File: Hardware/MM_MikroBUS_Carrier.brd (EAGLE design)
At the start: 85.1 x 35.6 mm, 90 parts, among them J15 MICROMOD-2222-C, J2 QWIIC_RIGHT_ANGLE, J5 Vertical Qwiic Connector, J7 MIKROBUS_SMD_BLACK1, U1 MCP73831, U2 AP7361C-33FGEUDFN-8

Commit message: Add HW test sketch
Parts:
- moved U$17 2.54 mm to (33.0, 30.5)
- moved U$18 2.54 mm to (33.0, 30.5)
- moved U$20 2.54 mm to (30.5, 30.7)
- moved U$21 2.54 mm to (30.5, 30.7)
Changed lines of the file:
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@@
 <?xml version="1.0" encoding="utf-8"?>
 <!DOCTYPE eagle SYSTEM "eagle.dtd">
-<eagle version="9.4.2">
+<eagle version="9.5.2">
 <drawing>
 <settings>
-<setting alwaysvectorfont="yes"/>
+<setting alwaysvectorfont="no"/>
 <setting verticaltext="up"/>
 </settings>
@@
 <layer number="23" name="tOrigins" color="15" fill="1" visible="yes" active="yes"/>
 <layer number="24" name="bOrigins" color="15" fill="1" visible="yes" active="yes"/>
-<layer number="25" name="tNames" color="7" fill="1" visible="yes" active="yes"/>
+<layer number="25" name="tNames" color="7" fill="1" visible="no" active="yes"/>
 <layer number="26" name="bNames" color="7" fill="1" visible="no" active="yes"/>
-<layer number="27" name="tValues" color="7" fill="1" visible="yes" active="yes"/>
+<layer number="27" name="tValues" color="7" fill="1" visible="no" active="yes"/>
 <layer number="28" name="bValues" color="7" fill="1" visible="no" active="yes"/>
 <layer number="29" name="tStop" color="7" fill="3" visible="no" active="yes"/>
@@
 <element name="U$36" library="buzzard_labels (1)" package="#0" value="" x="1.143" y="17.399" smashed="yes"/>
 <element name="U$37" library="buzzard_labels (1)" package="#0" value="" x="7.366" y="23.495" smashed="yes"/>
-<element name="U$17" library="output" package="#D0#0" value="" x="30.48" y="30.48" smashed="yes" rot="R90"/>
-<element name="U$18" library="output" package="#D0#0" value="" x="30.48" y="30.48" smashed="yes" rot="MR90"/>
-<element name="U$20" library="output" package="#D1#0" value="" x="33.02" y="30.734" smashed="yes" rot="R90"/>
-<element name="U$21" library="output" package="#D1#0" value="" x="33.02" y="30.734" smashed="yes" rot="MR90"/>
+<element name="U$17" library="output" package="#D0#0" value="" x="33.02" y="30.48" smashed="yes" rot="R90"/>
+<element name="U$18" library="output" package="#D0#0" value="" x="33.02" y="30.48" smashed="yes" rot="MR90"/>
+<element name="U$20" library="output" package="#D1#0" value="" x="30.48" y="30.734" smashed="yes" rot="R90"/>
+<element name="U$21" library="output" package="#D1#0" value="" x="30.48" y="30.734" smashed="yes" rot="MR90"/>
 <element name="J6" library="SparkFun-Connectors" package="1X09_NO_SILK" value="" x="22.86" y="34.29" smashed="yes">
 <attribute name="NAME" x="21.59" y="35.687" size="0.6096" layer="25" font="vector" ratio="20"/>

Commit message: Updating with mikroE suggestions
* "mikroBUS" label, not "MikroBUS"
* Add pin names to socket
* Change button labeling to "Mikroe Reset"
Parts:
- added U$1: (no value), output:MIKROE0
- added U$40: (no value), output:RST0
- added U$41: (no value), output:CS0
- added U$42: (no value), output:SCK0
- added U$43: (no value), output:CIPO0
- added U$45: (no value), output:COPI0
- added U$46: (no value), output:3#3V0
- added U$47, U$48: (no value), output:GND0
- added U$49: (no value), output:PWM0
- added U$50: (no value), output:INT0
- added U$51: (no value), output:RX0
- added U$52: (no value), output:TX0
- added U$53: (no value), output:SCL0
- added U$54: (no value), output:SDA0
- added U$55: (no value), output:VIN0
- U$35: device output:MIKROBUS_CARRIER0 -> output:AN0
- U$5: device output:MIK0 -> output:MIKROBUS_CARRIER0
- moved U$5 29.8 mm to (57.5, 1.65), turned to 0 degrees
- moved U$38 23.7 mm to (76.8, 15.1), flipped to the bottom
- moved U$35 11.6 mm to (74.9, 26.7), flipped to the top, turned to 270 degrees
- moved LOGO2 0.25 mm to (55.3, 1.65)
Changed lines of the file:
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@@
 <?xml version="1.0" encoding="utf-8"?>
 <!DOCTYPE eagle SYSTEM "eagle.dtd">
-<eagle version="9.5.2">
+<eagle version="9.4.2">
 <drawing>
 <settings>
-<setting alwaysvectorfont="no"/>
+<setting alwaysvectorfont="yes"/>
 <setting verticaltext="up"/>
 </settings>
@@
 <attribute name="VALUE" x="23.495" y="5.969" size="0.6096" layer="27" font="vector" ratio="20" rot="R180" align="top-center"/>
 </element>
-<element name="LOGO2" library="SparkFun-Aesthetics" package="QWIIC_5.5MM" value="QWIIC_LOGO_CONNECTOR" x="55.3085" y="1.397" smashed="yes"/>
+<element name="LOGO2" library="SparkFun-Aesthetics" package="QWIIC_5.5MM" value="QWIIC_LOGO_CONNECTOR" x="55.3085" y="1.651" smashed="yes"/>
 <element name="LOGO3" library="SparkFun-Aesthetics" package="OSHW-LOGO-M" value="OSHW-LOGOM" x="62.23" y="9.906" smashed="yes" rot="MR0"/>
 <element name="H5" library="SparkFun-Hardware" package="STAND-OFF-REFLOW-M2.5" value="STAND-OFF-REFLOW-M2.5_2.5MM_TALL" x="44.327" y="13.76" smashed="yes">
@@
 <element name="U$19" library="output" package="#3V3_#0" value="" x="20.828" y="33.655" smashed="yes" rot="MR0"/>
 <element name="U$6" library="output" package="#3V3_EN#0" value="" x="15.748" y="16.51" smashed="yes" rot="MR0"/>
-<element name="U$35" library="output" package="MIKROBUS_CARRIER0" value="" x="74.422" y="15.113" smashed="yes" rot="MR0"/>
-<element name="U$38" library="output" package="_MIKROBUS_CARRIER0" value="" x="57.277" y="1.651" smashed="yes"/>
-<element name="U$5" library="output" package="MIK0" value="" x="27.686" y="1.397" smashed="yes" rot="R90"/>
 <element name="U$39" library="output" package="RESET0" value="" x="28.829" y="0.508" smashed="yes" rot="R90"/>
+<element name="U$1" library="output" package="MIKROE0" value="" x="27.686" y="0.127" smashed="yes" rot="R90"/>
+<element name="U$5" library="output" package="MIKROBUS_CARRIER0" value="" x="57.531" y="1.651" smashed="yes"/>
+<element name="U$38" library="output" package="_MIKROBUS_CARRIER0" value="" x="76.835" y="15.113" smashed="yes" rot="MR0"/>
+<element name="U$35" library="output" package="AN0" value="" x="74.93" y="26.67" smashed="yes" rot="R270"/>
+<element name="U$40" library="output" package="RST0" value="" x="72.39" y="26.67" smashed="yes" rot="R270"/>
+<element name="U$41" library="output" package="CS0" value="" x="69.85" y="26.67" smashed="yes" rot="R270"/>
+<element name="U$42" library="output" package="SCK0" value="" x="67.31" y="26.67" smashed="yes" rot="R270"/>
+<element name="U$43" library="output" package="CIPO0" value="" x="64.77" y="26.67" smashed="yes" rot="R270"/>
+<element name="U$45" library="output" package="COPI0" value="" x="62.23" y="26.67" smashed="yes" rot="R270"/>
+<element name="U$46" library="output" package="3#3V0" value="" x="59.69" y="26.67" smashed="yes" rot="R270"/>
+<element name="U$47" library="output" package="GND0" value="" x="57.15" y="26.67" smashed="yes" rot="R270"/>
+<element name="U$48" library="output" package="GND0" value="" x="57.15" y="12.954" smashed="yes" rot="R270"/>
+<element name="U$49" library="output" package="PWM0" value="" x="74.93" y="13.589" smashed="yes" rot="R270"/>
+<element name="U$50" library="output" package="INT0" value="" x="72.39" y="12.446" smashed="yes" rot="R270"/>
+<element name="U$51" library="output" package="RX0" value="" x="69.85" y="11.938" smashed="yes" rot="R270"/>
+<element name="U$52" library="output" package="TX0" value="" x="67.31" y="12.192" smashed="yes" rot="R270"/>
+<element name="U$53" library="output" package="SCL0" value="" x="64.77" y="12.7" smashed="yes" rot="R270"/>
+<element name="U$54" library="output" package="SDA0" value="" x="62.23" y="12.954" smashed="yes" rot="R270"/>
+<element name="U$55" library="output" package="VIN0" value="" x="59.69" y="12.573" smashed="yes" rot="R270"/>
 </elements>
 <signals>
@@
 <contactref element="S3" pad="2"/>
 <via x="57.15" y="28.321" extent="1-16" drill="0.3048"/>
-<via x="57.15" y="6.858" extent="1-16" drill="0.3048"/>
+<via x="58.039" y="2.921" extent="1-16" drill="0.3048"/>
 <via x="33.02" y="1.27" extent="1-16" drill="0.3048"/>
 <via x="50.292" y="2.286" extent="1-16" drill="0.3048"/>

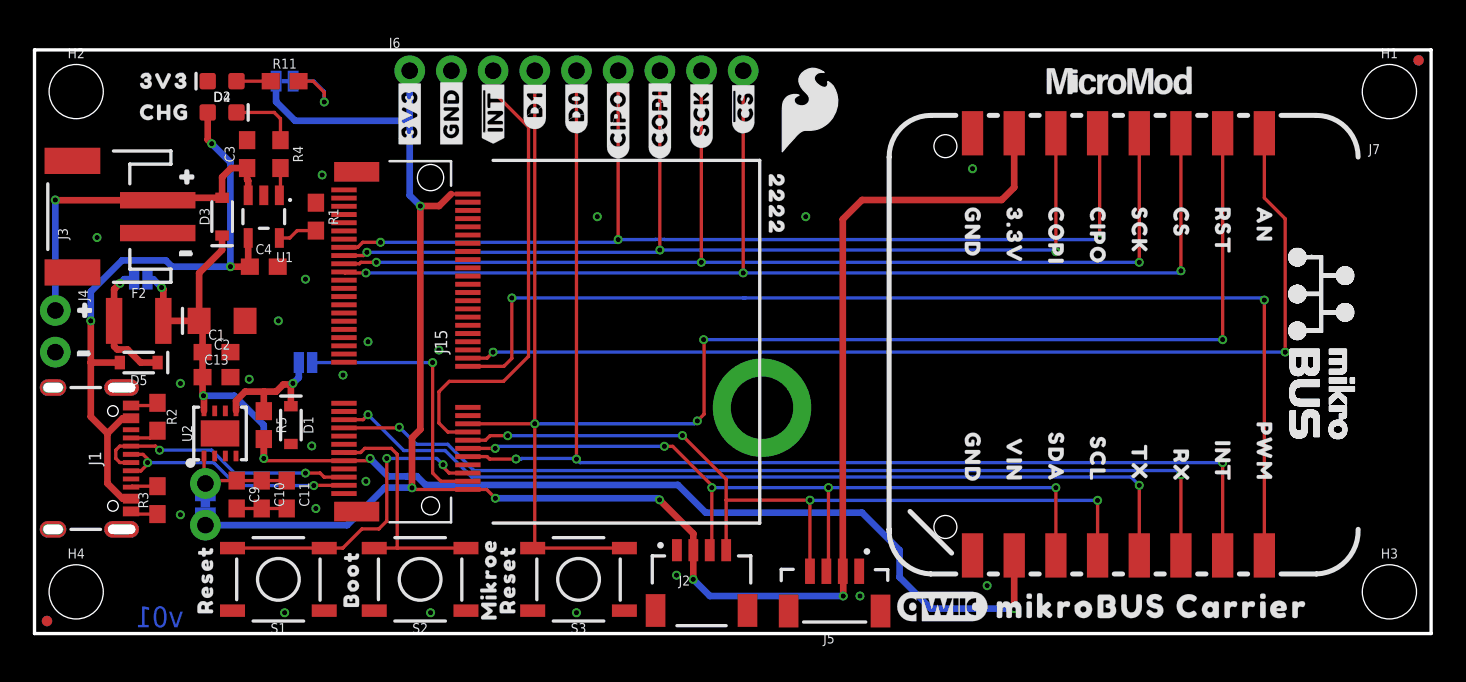
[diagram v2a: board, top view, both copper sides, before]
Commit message: MikroE updates
* Add JTAG connector
* Remove mikroE reset button
* Moved mikroBUS labels so that they can all be seen when socket is populated
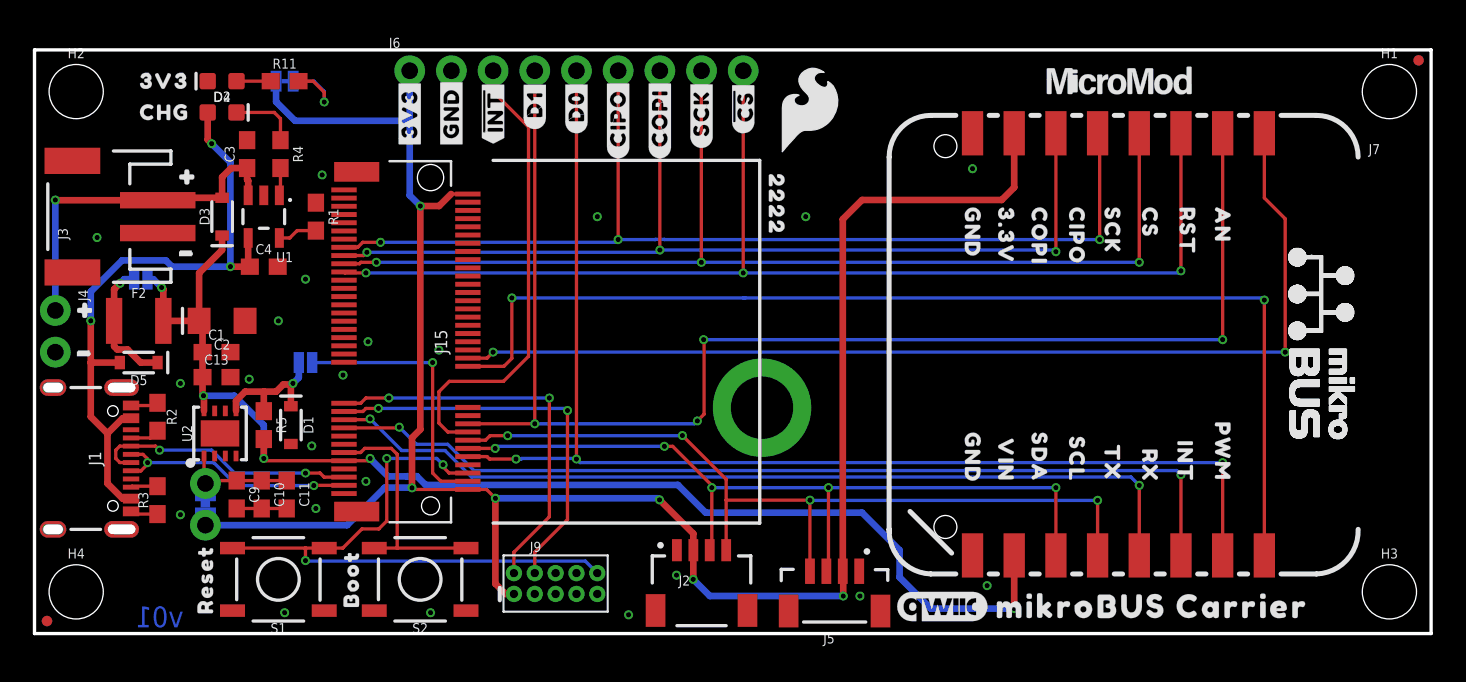
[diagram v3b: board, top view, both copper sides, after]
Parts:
- removed S3: MIK_RESET, SparkFun-Switches:TACTILE_SWITCH_SMD_5.2MM
- removed U$1: (no value), output:MIKROE0
- removed U$39: (no value), output:RESET0
- added J9: CORTEX_JTAG_DEBUG_MINIMUM_PTH, SparkFun-Connectors:2X5-PTH-1.27MM
- moved U$35 2.54 mm to (72.4, 26.7)
- moved U$49 2.54 mm to (72.4, 13.6)
- moved U$50 2.29 mm to (70.1, 12.4)
- moved U$40 2.16 mm to (70.2, 26.7)
- moved U$41 1.91 mm to (67.9, 26.7)
- moved U$51 1.91 mm to (67.9, 11.9)
- moved U$42 1.65 mm to (65.7, 26.7)
- moved U$52 1.65 mm to (65.7, 12.2)
- moved U$43 1.27 mm to (63.5, 26.7)
- moved U$53 1.27 mm to (63.5, 12.7)
- moved U$45 1.02 mm to (61.2, 26.7)
- moved U$54 1.02 mm to (61.2, 13.0)
- moved U$46 0.51 mm to (59.2, 26.7)
- moved U$55 0.51 mm to (59.2, 12.6)
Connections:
- new net SWDCK: J15.21, J9.4
- new net SWDIO: J15.23, J9.2
- net !RESET!: now also J9.10
- net 3.3V: now also J9.1
- net GND: now also J9.3, J9.5, J9.9; no longer S3.1, S3.2
- net MIK_RST: no longer S3.3, S3.4
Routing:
- net SWDCK: track 0.00 -> 24.5 mm, vias 0 -> 2
- net SWDIO: track 0.00 -> 24.2 mm, vias 0 -> 2
- net !RESET!: track 19.3 -> 38.1 mm, vias 2 -> 3
- net MIK_RST: track 98.1 -> 84.9 mm
- net 3.3V: track 121.4 -> 128.0 mm

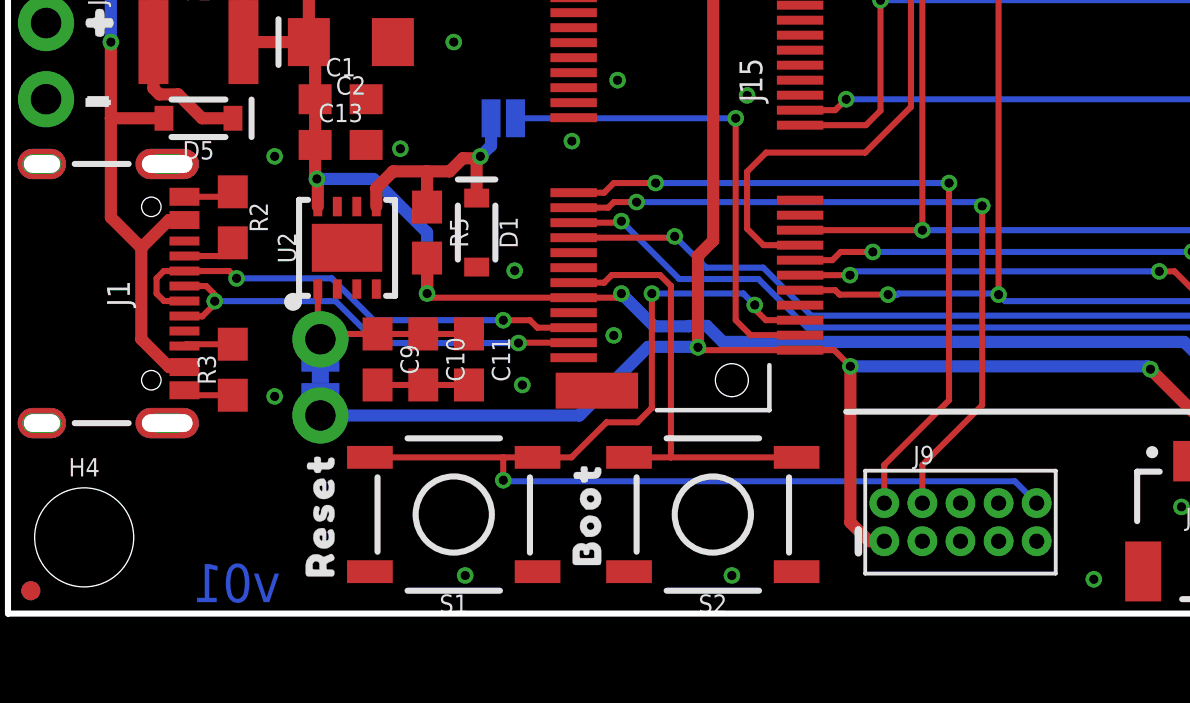
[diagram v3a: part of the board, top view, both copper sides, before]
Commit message: Pete's updates
* Bump version number on schematic and board
* Add measures for header
* Add test points for SWDIO and SWDCK
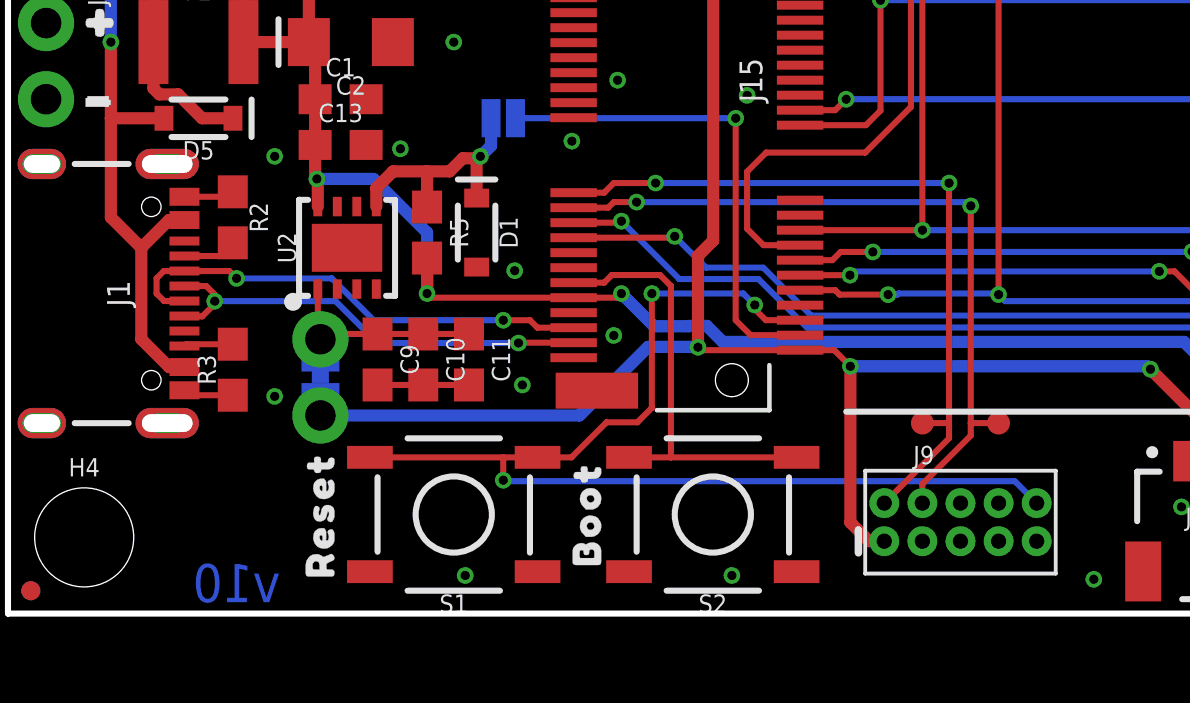
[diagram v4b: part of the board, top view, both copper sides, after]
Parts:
- added SWDCK, SWDIO: TEST-POINT3, SparkFun-Connectors:PAD.03X.03
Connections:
- net SWDCK: now also SWDCK.1
- net SWDIO: now also SWDIO.1
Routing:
- net SWDIO: track 24.2 -> 25.1 mm
- net SWDCK: track 24.5 -> 25.1 mm
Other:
- board text added: "v10"
- board text removed: "v01"
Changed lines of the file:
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@@
 <layer number="45" name="Holes" color="7" fill="1" visible="yes" active="yes"/>
 <layer number="46" name="Milling" color="3" fill="1" visible="no" active="yes"/>
-<layer number="47" name="Measures" color="7" fill="1" visible="no" active="yes"/>
+<layer number="47" name="Measures" color="7" fill="1" visible="yes" active="yes"/>
 <layer number="48" name="Document" color="7" fill="1" visible="no" active="yes"/>
 <layer number="49" name="Reference" color="7" fill="1" visible="no" active="yes"/>
@@
 <wire x1="85.09" y1="35.56" x2="85.09" y2="0" width="0.2032" layer="20"/>
 <wire x1="85.09" y1="0" x2="0" y2="0" width="0.2032" layer="20"/>
-<text x="7.62" y="1.016" size="1.27" layer="16" font="vector" ratio="20" rot="MR180" align="center">v01</text>
+<text x="7.62" y="1.016" size="1.27" layer="16" font="vector" ratio="20" rot="MR180" align="center">v10</text>
 <wire x1="27.94" y1="28.829" x2="44.185" y2="28.829" width="0.2032" layer="21"/>
 <wire x1="44.185" y1="28.829" x2="44.185" y2="6.731" width="0.2032" layer="21"/>
@@
 <text x="93.091" y="22.86" size="1.778" layer="47" font="vector" ratio="15" rot="R270">in</text>
 <text x="85.344" y="16.637" size="1.778" layer="47" font="vector" ratio="15" rot="R270">in</text>
-<text x="45.974" y="38.735" size="1.778" layer="47" font="vector" ratio="15">in</text>
-<text x="45.974" y="43.688" size="1.778" layer="47" font="vector" ratio="15">in</text>
+<text x="45.974" y="45.085" size="1.778" layer="47" font="vector" ratio="15">in</text>
+<text x="45.974" y="41.148" size="1.778" layer="47" font="vector" ratio="15">in</text>
 <dimension x1="0" y1="0" x2="6.223" y2="10.668" x3="-2.54" y3="5.334" textsize="1.778" textratio="15" layer="47" dtype="vertical" unit="inch"/>
 <dimension x1="0" y1="0" x2="3.81" y2="25.4" x3="-6.35" y3="12.7" textsize="1.778" textratio="15" layer="47" dtype="vertical" unit="inch"/>
 <text x="-6.858" y="16.129" size="1.778" layer="47" font="vector" ratio="15" rot="R90">in</text>
 <text x="-3.175" y="8.509" size="1.778" layer="47" font="vector" ratio="15" rot="R90">in</text>
-<dimension x1="2.54" y1="33.02" x2="82.55" y2="33.02" x3="42.545" y3="38.1" textsize="1.778" textratio="15" layer="47" unit="inch"/>
-<dimension x1="0" y1="35.56" x2="85.09" y2="35.56" x3="42.545" y3="43.18" textsize="1.778" textratio="15" layer="47" unit="inch"/>
+<dimension x1="2.54" y1="33.02" x2="82.55" y2="33.02" x3="42.545" y3="40.64" textsize="1.778" textratio="15" layer="47" unit="inch"/>
+<dimension x1="0" y1="35.56" x2="85.09" y2="35.56" x3="42.545" y3="44.45" textsize="1.778" textratio="15" layer="47" unit="inch"/>
+<dimension x1="0" y1="35.56" x2="22.86" y2="35.56" x3="11.43" y3="36.83" textsize="1.778" textratio="15" layer="47" unit="inch"/>
+<text x="14.224" y="37.465" size="1.778" layer="47" font="vector" ratio="15">in</text>
 </plain>
 <attributes>
@@
 <attribute name="VALUE" x="29.9212" y="0.5842" size="0.6096" layer="27" font="vector" ratio="20"/>
 </element>
+<element name="SWDCK" library="SparkFun-Connectors" package="PAD.03X.03" value="TEST-POINT3" x="33.02" y="6.35" smashed="yes"/>
+<element name="SWDIO" library="SparkFun-Connectors" package="PAD.03X.03" value="TEST-POINT3" x="30.48" y="6.35" smashed="yes"/>
 </elements>
 <signals>
@@
 <wire x1="21.59" y1="14.351" x2="31.369" y2="14.351" width="0.2032" layer="16"/>
 <via x="31.369" y="14.351" extent="1-16" drill="0.3048"/>
-<wire x1="31.369" y1="14.351" x2="31.369" y2="7.112" width="0.2032" layer="1"/>
-<wire x1="31.369" y1="7.112" x2="29.21" y2="4.953" width="0.2032" layer="1"/>
-<wire x1="29.21" y1="4.953" x2="29.21" y2="3.683" width="0.2032" layer="1"/>
+<wire x1="31.369" y1="14.351" x2="31.369" y2="6.35" width="0.2032" layer="1"/>
+<wire x1="31.369" y1="6.35" x2="31.369" y2="5.842" width="0.2032" layer="1"/>
+<wire x1="31.369" y1="5.842" x2="29.21" y2="3.683" width="0.2032" layer="1"/>
+<contactref element="SWDIO" pad="1"/>
+<wire x1="30.48" y1="6.35" x2="31.369" y2="6.35" width="0.2032" layer="1"/>
 </signal>
 <signal name="SWDCK">
@@
 <wire x1="20.193" y1="13.716" x2="20.955" y2="13.716" width="0.2032" layer="1"/>
 <via x="20.955" y="13.716" extent="1-16" drill="0.3048"/>
-<wire x1="32.385" y1="13.716" x2="20.955" y2="13.716" width="0.2032" layer="16"/>
-<via x="32.4739" y="13.589" extent="1-16" drill="0.3048"/>
-<wire x1="32.4739" y1="13.589" x2="32.4739" y2="6.9469" width="0.2032" layer="1"/>
-<wire x1="32.4739" y1="6.9469" x2="30.48" y2="4.953" width="0.2032" layer="1"/>
-<wire x1="30.48" y1="4.953" x2="30.48" y2="3.683" width="0.2032" layer="1"/>
-<wire x1="32.4739" y1="13.589" x2="32.385" y2="13.6779" width="0.2032" layer="16"/>
-<wire x1="32.385" y1="13.6779" x2="32.385" y2="13.716" width="0.2032" layer="16"/>
+<wire x1="32.2199" y1="13.716" x2="20.955" y2="13.716" width="0.2032" layer="16"/>
+<via x="32.0929" y="13.589" extent="1-16" drill="0.3048"/>
+<wire x1="32.0929" y1="13.589" x2="32.0929" y2="6.35" width="0.2032" layer="1"/>
+<wire x1="32.0929" y1="6.35" x2="32.0929" y2="5.9309" width="0.2032" layer="1"/>
+<wire x1="32.0929" y1="5.9309" x2="30.48" y2="4.318" width="0.2032" layer="1"/>
+<wire x1="30.48" y1="4.318" x2="30.48" y2="3.683" width="0.2032" layer="1"/>
+<wire x1="32.0929" y1="13.589" x2="32.2199" y2="13.716" width="0.2032" layer="16"/>
+<contactref element="SWDCK" pad="1"/>
+<wire x1="32.0929" y1="6.35" x2="33.02" y2="6.35" width="0.2032" layer="1"/>
 </signal>
 </signals>
